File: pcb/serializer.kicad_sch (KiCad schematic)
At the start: 28 parts, among them U7 DS90UB953A-Q1

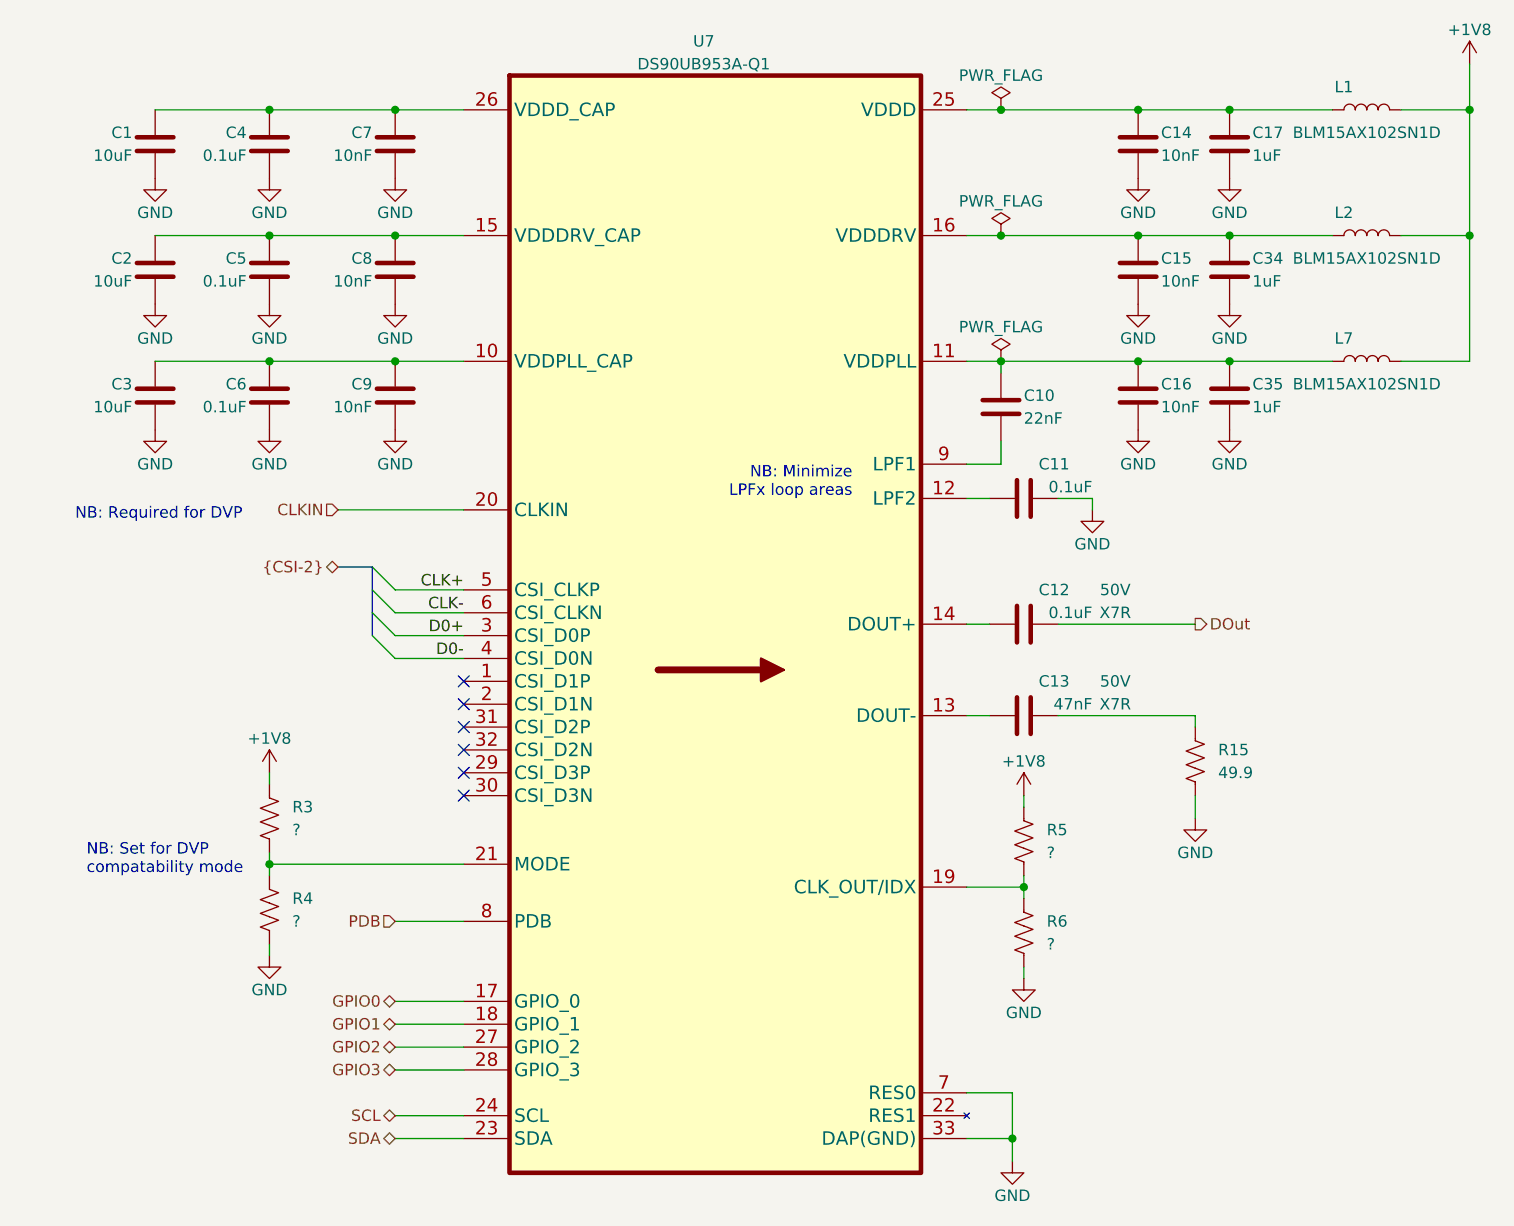
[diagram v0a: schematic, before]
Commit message: Rev. A initial design prior to fab comments
- BOM simplification
- Added my initials to the board
- Made the board more easy to panlize
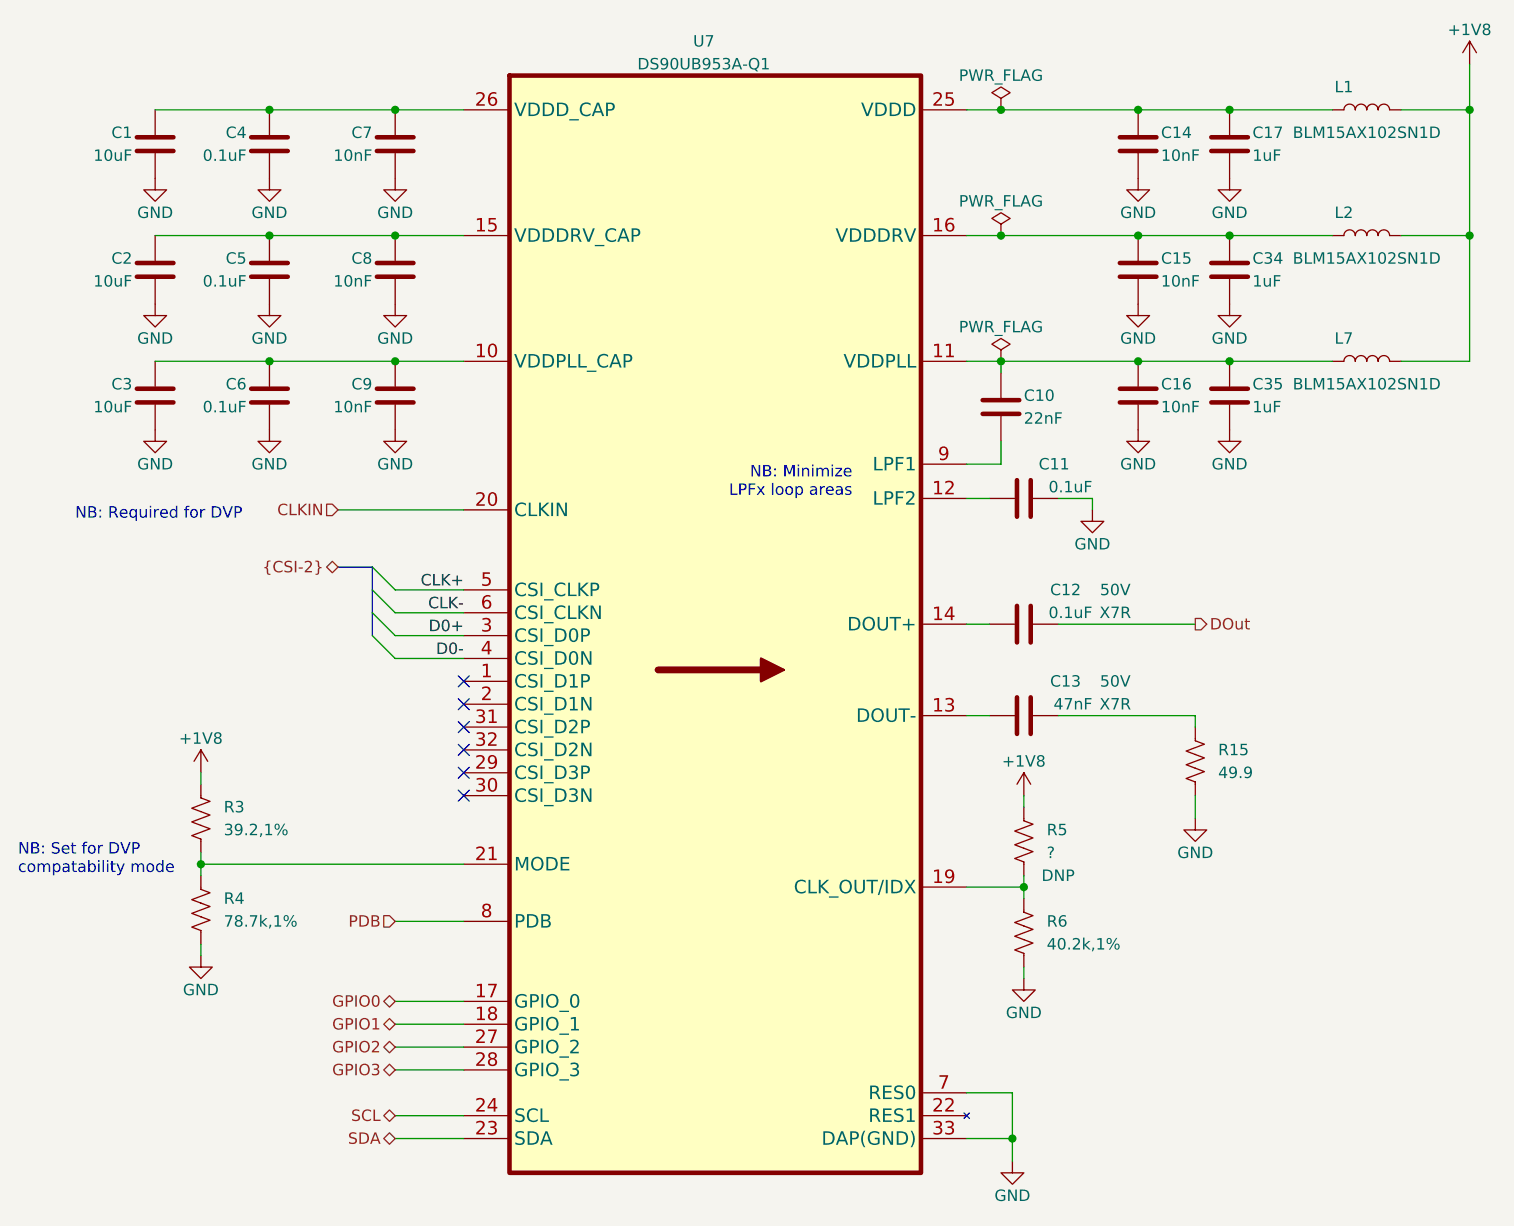
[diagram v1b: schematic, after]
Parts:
- R3: value ? -> 39.2,1%
- R4: value ? -> 78.7k,1%
- R5: DNP (none) -> DNP; now left out of the parts list
- R6: value ? -> 40.2k,1%
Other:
- moved on the sheet: R3, R4
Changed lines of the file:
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@@
   (junction (at 86.36 59.69) (diameter 0) (color 0 0 0 0)
   )
-  (junction (at 86.36 129.54) (diameter 0) (color 0 0 0 0)
+  (junction (at 78.74 129.54) (diameter 0) (color 0 0 0 0)
   )
   (junction (at 167.64 73.66) (diameter 0) (color 0 0 0 0)
@@
     (stroke (width 0) (type default) (color 0 0 0 0))
   )
-  (wire (pts (xy 86.36 129.54) (xy 107.95 129.54))
+  (wire (pts (xy 78.74 129.54) (xy 107.95 129.54))
     (stroke (width 0) (type default) (color 0 0 0 0))
   )
@@
     (stroke (width 0) (type default) (color 0 0 0 0))
   )
-  (wire (pts (xy 86.36 119.38) (xy 86.36 120.65))
+  (wire (pts (xy 78.74 119.38) (xy 78.74 120.65))
     (stroke (width 0) (type default) (color 0 0 0 0))
   )
@@
     (stroke (width 0) (type default) (color 0 0 0 0))
   )
-  (wire (pts (xy 86.36 128.27) (xy 86.36 129.54))
-    (stroke (width 0) (type default) (color 0 0 0 0))
-  )
-  (wire (pts (xy 86.36 129.54) (xy 86.36 130.81))
+  (wire (pts (xy 78.74 128.27) (xy 78.74 129.54))
+    (stroke (width 0) (type default) (color 0 0 0 0))
+  )
+  (wire (pts (xy 78.74 129.54) (xy 78.74 130.81))
     (stroke (width 0) (type default) (color 0 0 0 0))
   )
@@
     (stroke (width 0) (type default) (color 0 0 0 0))
   )
-  (wire (pts (xy 86.36 138.43) (xy 86.36 139.7))
+  (wire (pts (xy 78.74 138.43) (xy 78.74 139.7))
     (stroke (width 0) (type default) (color 0 0 0 0))
   )
@@
     (stroke (width 0) (type default) (color 0 0 0 0))
   )
-  (text "NB: Set for DVP\ncompatability mode" (at 66.04 130.81 0)
+  (text "NB: Set for DVP\ncompatability mode" (at 58.42 130.81 0)
     (effects (font (size 1.27 1.27)) (justify left bottom))
   )
@@
   (symbol (lib_id "Device:C") (at 170.18 113.03 90) (unit 1)
     (in_bom yes) (on_board yes)
-    (property "Reference" "C13" (id 0) (at 175.26 109.22 90)
+    (property "Reference" "C13" (id 0) (at 176.53 109.22 90)
       (effects (font (size 1.27 1.27)) (justify left))
     )
@@
     (pin "2")
   )
-  (symbol (lib_id "power:GND") (at 86.36 139.7 0) (unit 1)
-    (in_bom yes) (on_board yes)
-    (property "Reference" "#PWR0132" (id 0) (at 86.36 146.05 0)
-      (effects (font (size 1.27 1.27)) hide)
-    )
-    (property "Value" "GND" (id 1) (at 86.36 143.51 0))
-    (property "Footprint" "" (id 2) (at 86.36 139.7 0)
-      (effects (font (size 1.27 1.27)) hide)
-    )
-    (property "Datasheet" "" (id 3) (at 86.36 139.7 0)
+  (symbol (lib_id "power:GND") (at 78.74 139.7 0) (unit 1)
+    (in_bom yes) (on_board yes)
+    (property "Reference" "#PWR0132" (id 0) (at 78.74 146.05 0)
+      (effects (font (size 1.27 1.27)) hide)
+    )
+    (property "Value" "GND" (id 1) (at 78.74 143.51 0))
+    (property "Footprint" "" (id 2) (at 78.74 139.7 0)
+      (effects (font (size 1.27 1.27)) hide)
+    )
+    (property "Datasheet" "" (id 3) (at 78.74 139.7 0)
       (effects (font (size 1.27 1.27)) hide)
     )
@@
     (pin "2")
   )
-  (symbol (lib_id "Device:R_US") (at 86.36 134.62 0) (unit 1)
-    (in_bom yes) (on_board yes)
-    (property "Reference" "R4" (id 0) (at 88.9 133.35 0)
-      (effects (font (size 1.27 1.27)) (justify left))
-    )
-    (property "Value" "?" (id 1) (at 88.9 135.89 0)
-      (effects (font (size 1.27 1.27)) (justify left))
-    )
-    (property "Footprint" "Resistor_SMD:R_0201_0603Metric" (id 2) (at 87.376 134.874 90)
-      (effects (font (size 1.27 1.27)) hide)
-    )
-    (property "Datasheet" "~" (id 3) (at 86.36 134.62 0)
+  (symbol (lib_id "Device:R_US") (at 78.74 134.62 0) (unit 1)
+    (in_bom yes) (on_board yes)
+    (property "Reference" "R4" (id 0) (at 81.28 133.35 0)
+      (effects (font (size 1.27 1.27)) (justify left))
+    )
+    (property "Value" "78.7k,1%" (id 1) (at 81.28 135.89 0)
+      (effects (font (size 1.27 1.27)) (justify left))
+    )
+    (property "Footprint" "Resistor_SMD:R_0201_0603Metric" (id 2) (at 79.756 134.874 90)
+      (effects (font (size 1.27 1.27)) hide)
+    )
+    (property "Datasheet" "~" (id 3) (at 78.74 134.62 0)
       (effects (font (size 1.27 1.27)) hide)
     )
@@
     (pin "1")
   )
-  (symbol (lib_id "power:+1V8") (at 86.36 119.38 0) (unit 1)
-    (in_bom yes) (on_board yes)
-    (property "Reference" "#PWR0133" (id 0) (at 86.36 123.19 0)
-      (effects (font (size 1.27 1.27)) hide)
-    )
-    (property "Value" "+1V8" (id 1) (at 86.36 115.57 0))
-    (property "Footprint" "" (id 2) (at 86.36 119.38 0)
-      (effects (font (size 1.27 1.27)) hide)
-    )
-    (property "Datasheet" "" (id 3) (at 86.36 119.38 0)
+  (symbol (lib_id "power:+1V8") (at 78.74 119.38 0) (unit 1)
+    (in_bom yes) (on_board yes)
+    (property "Reference" "#PWR0133" (id 0) (at 78.74 123.19 0)
+      (effects (font (size 1.27 1.27)) hide)
+    )
+    (property "Value" "+1V8" (id 1) (at 78.74 115.57 0))
+    (property "Footprint" "" (id 2) (at 78.74 119.38 0)
+      (effects (font (size 1.27 1.27)) hide)
+    )
+    (property "Datasheet" "" (id 3) (at 78.74 119.38 0)
       (effects (font (size 1.27 1.27)) hide)
     )
@@
   )
   (symbol (lib_id "Device:R_US") (at 170.18 127 0) (unit 1)
-    (in_bom yes) (on_board yes)
+    (in_bom no) (on_board yes)
     (property "Reference" "R5" (id 0) (at 172.72 125.73 0)
       (effects (font (size 1.27 1.27)) (justify left))
@@
       (effects (font (size 1.27 1.27)) hide)
     )
+    (property "DNP" "DNP" (id 4) (at 173.99 130.81 0))
     (pin "1")
     (pin "2")
@@
   (symbol (lib_id "Device:C") (at 170.18 102.87 90) (unit 1)
     (in_bom yes) (on_board yes)
-    (property "Reference" "C12" (id 0) (at 175.26 99.06 90)
+    (property "Reference" "C12" (id 0) (at 176.53 99.06 90)
       (effects (font (size 1.27 1.27)) (justify left))
     )
@@
     (pin "2")
   )
-  (symbol (lib_id "Device:R_US") (at 86.36 124.46 0) (unit 1)
-    (in_bom yes) (on_board yes)
-    (property "Reference" "R3" (id 0) (at 88.9 123.19 0)
-      (effects (font (size 1.27 1.27)) (justify left))
-    )
-    (property "Value" "?" (id 1) (at 88.9 125.73 0)
-      (effects (font (size 1.27 1.27)) (justify left))
-    )
-    (property "Footprint" "Resistor_SMD:R_0201_0603Metric" (id 2) (at 87.376 124.714 90)
-      (effects (font (size 1.27 1.27)) hide)
-    )
-    (property "Datasheet" "~" (id 3) (at 86.36 124.46 0)
+  (symbol (lib_id "Device:R_US") (at 78.74 124.46 0) (unit 1)
+    (in_bom yes) (on_board yes)
+    (property "Reference" "R3" (id 0) (at 81.28 123.19 0)
+      (effects (font (size 1.27 1.27)) (justify left))
+    )
+    (property "Value" "39.2,1%" (id 1) (at 81.28 125.73 0)
+      (effects (font (size 1.27 1.27)) (justify left))
+    )
+    (property "Footprint" "Resistor_SMD:R_0201_0603Metric" (id 2) (at 79.756 124.714 90)
+      (effects (font (size 1.27 1.27)) hide)
+    )
+    (property "Datasheet" "~" (id 3) (at 78.74 124.46 0)
       (effects (font (size 1.27 1.27)) hide)
     )
@@
       (effects (font (size 1.27 1.27)) (justify left))
     )
-    (property "Value" "?" (id 1) (at 172.72 138.43 0)
-      (effects (font (size 1.27 1.27)) (justify left))
-    )
+    (property "Value" "40.2k,1%" (id 1) (at 172.72 138.43 0)
+      (effects (font (size 1.27 1.27)) (justify left))
+    )

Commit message: Start of revision B
- Address the following issues
1. The photodiode anode is on pin 3, not pin 2
2. No paste on coax connector
3. CRESET_B needs to come out to programming header
4. Need PU on CS line.
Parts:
- C1, C2, C3: TempCo (none) -> X5R; Voltage (none) -> 10V
- C10, C14, C15, C16, C7, C8, C9: TempCo (none) -> X7R; Voltage (none) -> 35V
- C11, C4, C5, C6: TempCo (none) -> X7R; Voltage (none) -> 16V
- C17, C34, C35: TempCo (none) -> X5R; Voltage (none) -> 16V
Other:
- title: Headstage-RHS2116 -> Headstage-64s
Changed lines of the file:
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@@
   (paper "A4")
   (title_block
-    (title "Headstage-RHS2116")
+    (title "Headstage-64s")
     (date "2021-12-16")
-    (rev "A")
+    (rev "B")
     (company "Open Ephys, Inc")
     (comment 1 "Jonathan P. Newman")
@@
       (effects (font (size 1.27 1.27)) hide)
     )
+    (property "TempCo" "X5R" (id 4) (at 193.04 49.53 0)
+      (effects (font (size 1.27 1.27)) hide)
+    )
+    (property "Voltage" "16V" (id 5) (at 193.04 49.53 0)
+      (effects (font (size 1.27 1.27)) hide)
+    )
     (pin "1")
     (pin "2")
@@
       (effects (font (size 1.27 1.27)) hide)
     )
+    (property "TempCo" "X7R" (id 4) (at 182.88 77.47 0)
+      (effects (font (size 1.27 1.27)) hide)
+    )
+    (property "Voltage" "35V" (id 5) (at 182.88 77.47 0)
+      (effects (font (size 1.27 1.27)) hide)
+    )
     (pin "1")
     (pin "2")
@@
       (effects (font (size 1.27 1.27)) hide)
     )
+    (property "TempCo" "X5R" (id 4) (at 73.66 77.47 0)
+      (effects (font (size 1.27 1.27)) hide)
+    )
+    (property "Voltage" "10V" (id 5) (at 73.66 77.47 0)
+      (effects (font (size 1.27 1.27)) hide)
+    )
     (pin "1")
     (pin "2")
@@
       (effects (font (size 1.27 1.27)) hide)
     )
+    (property "TempCo" "X7R" (id 4) (at 182.88 49.53 0)
+      (effects (font (size 1.27 1.27)) hide)
+    )
+    (property "Voltage" "35V" (id 5) (at 182.88 49.53 0)
+      (effects (font (size 1.27 1.27)) hide)
+    )
     (pin "1")
     (pin "2")
@@
     )
     (property "Datasheet" "~" (id 3) (at 100.33 77.47 0)
+      (effects (font (size 1.27 1.27)) hide)
+    )
+    (property "TempCo" "X7R" (id 4) (at 100.33 77.47 0)
+      (effects (font (size 1.27 1.27)) hide)
+    )
+    (property "Voltage" "35V" (id 5) (at 100.33 77.47 0)
       (effects (font (size 1.27 1.27)) hide)
     )
@@
     )
     (property "Datasheet" "~" (id 3) (at 86.36 63.5 0)
+      (effects (font (size 1.27 1.27)) hide)
+    )
+    (property "TempCo" "X7R" (id 4) (at 86.36 63.5 0)
+      (effects (font (size 1.27 1.27)) hide)
+    )
+    (property "Voltage" "16V" (id 5) (at 86.36 63.5 0)
       (effects (font (size 1.27 1.27)) hide)
     )
@@
       (effects (font (size 1.27 1.27)) hide)
     )
+    (property "TempCo" "X7R" (id 4) (at 100.33 49.53 0)
+      (effects (font (size 1.27 1.27)) hide)
+    )
+    (property "Voltage" "35V" (id 5) (at 100.33 49.53 0)
+      (effects (font (size 1.27 1.27)) hide)
+    )
     (pin "1")
     (pin "2")
@@
       (effects (font (size 1.27 1.27)) hide)
     )
+    (property "TempCo" "X5R" (id 4) (at 73.66 63.5 0)
+      (effects (font (size 1.27 1.27)) hide)
+    )
+    (property "Voltage" "10V" (id 5) (at 73.66 63.5 0)
+      (effects (font (size 1.27 1.27)) hide)
+    )
     (pin "1")
     (pin "2")
@@
     )
     (property "Datasheet" "~" (id 3) (at 86.36 77.47 0)
+      (effects (font (size 1.27 1.27)) hide)
+    )
+    (property "TempCo" "X7R" (id 4) (at 86.36 77.47 0)
+      (effects (font (size 1.27 1.27)) hide)
+    )
+    (property "Voltage" "16V" (id 5) (at 86.36 77.47 0)
       (effects (font (size 1.27 1.27)) hide)
     )
@@
       (effects (font (size 1.27 1.27)) hide)
     )
+    (property "TempCo" "X7R" (id 4) (at 86.36 49.53 0)
+      (effects (font (size 1.27 1.27)) hide)
+    )
+    (property "Voltage" "16V" (id 5) (at 86.36 49.53 0)
+      (effects (font (size 1.27 1.27)) hide)
+    )
     (pin "1")
     (pin "2")
@@
     )
     (property "Datasheet" "~" (id 3) (at 73.66 49.53 0)
+      (effects (font (size 1.27 1.27)) hide)
+    )
+    (property "TempCo" "X5R" (id 4) (at 73.66 49.53 0)
+      (effects (font (size 1.27 1.27)) hide)
+    )
+    (property "Voltage" "10V" (id 5) (at 73.66 49.53 0)
       (effects (font (size 1.27 1.27)) hide)
     )
@@
     )
     (property "Datasheet" "~" (id 3) (at 193.04 63.5 0)
+      (effects (font (size 1.27 1.27)) hide)
+    )
+    (property "TempCo" "X5R" (id 4) (at 193.04 63.5 0)
+      (effects (font (size 1.27 1.27)) hide)
+    )
+    (property "Voltage" "16V" (id 5) (at 193.04 63.5 0)
       (effects (font (size 1.27 1.27)) hide)
     )
@@
       (effects (font (size 1.27 1.27)) hide)
     )
-    (property "Datasheet" "" (id 3) (at 120.65 40.64 0)
+    (property "Datasheet" "~" (id 3) (at 120.65 40.64 0)
       (effects (font (size 1.27 1.27)) hide)
     )
@@
       (effects (font (size 1.27 1.27)) hide)
     )
+    (property "TempCo" "X7R" (id 4) (at 170.18 88.9 0)
+      (effects (font (size 1.27 1.27)) hide)
+    )
+    (property "Voltage" "16V" (id 5) (at 170.18 88.9 0)
+      (effects (font (size 1.27 1.27)) hide)
+    )
     (pin "1")
     (pin "2")
@@
     )
     (property "Datasheet" "~" (id 3) (at 193.04 77.47 0)
+      (effects (font (size 1.27 1.27)) hide)
+    )
+    (property "TempCo" "X5R" (id 4) (at 193.04 77.47 0)
+      (effects (font (size 1.27 1.27)) hide)
+    )
+    (property "Voltage" "16V" (id 5) (at 193.04 77.47 0)
       (effects (font (size 1.27 1.27)) hide)
     )
@@
       (effects (font (size 1.27 1.27)) hide)
     )
+    (property "TempCo" "X7R" (id 4) (at 100.33 63.5 0)
+      (effects (font (size 1.27 1.27)) hide)
+    )
+    (property "Voltage" "35V" (id 5) (at 100.33 63.5 0)
+      (effects (font (size 1.27 1.27)) hide)
+    )
     (pin "1")
     (pin "2")
@@
       (effects (font (size 1.27 1.27)) hide)
     )
+    (property "TempCo" "X7R" (id 4) (at 182.88 63.5 0)
+      (effects (font (size 1.27 1.27)) hide)
+    )
+    (property "Voltage" "35V" (id 5) (at 182.88 63.5 0)
+      (effects (font (size 1.27 1.27)) hide)
+    )
     (pin "1")
     (pin "2")
@@
       (effects (font (size 1.27 1.27)) hide)
     )
+    (property "TempCo" "X7R" (id 4) (at 167.64 78.74 0)
+      (effects (font (size 1.27 1.27)) hide)
+    )
+    (property "Voltage" "35V" (id 5) (at 167.64 78.74 0)
+      (effects (font (size 1.27 1.27)) hide)
+    )
